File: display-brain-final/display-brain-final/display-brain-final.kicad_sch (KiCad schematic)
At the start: 16 parts, among them J2 Conn_01x05_Socket, J3 Conn_01x19_Socket, J4 Conn_01x19_Socket, J5 Conn_01x04_Socket, J6 Conn_01x07_Socket, J7 Conn_01x02_Socket, P1 USB_C_Plug_USB2.0, U2 ESP32-WROOM-32, U3 AMS1117CD-3.3

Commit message: display brain platine fertig
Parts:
- added C1, C4: 10u, Capacitor_SMD:C_1206_3216Metric_Pad1.33x1.80mm_HandSolder, symbol Device:C_Polarized
- added C2, C3: 1u, Capacitor_SMD:C_1206_3216Metric_Pad1.33x1.80mm_HandSolder, symbol Device:C
- added D1: LED, Diode_SMD:D_1206_3216Metric_Pad1.42x1.75mm_HandSolder, symbol Device:LED
- added R2: 330, Resistor_SMD:R_1206_3216Metric_Pad1.30x1.75mm_HandSolder, symbol Device:R
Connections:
- net 3V3: now also C3.1, C4.1, D1.2 (A)
- net GND: now also C1.2, C2.2, C3.2, C4.2, R2.1
- net at P1.A4 (VBUS), P1.A9 (VBUS), P1.B4 (VBUS)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: now also C1.1, C2.1
- new net: D1.1 (K), R2.2
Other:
- moved on the sheet: J6, J7, U3

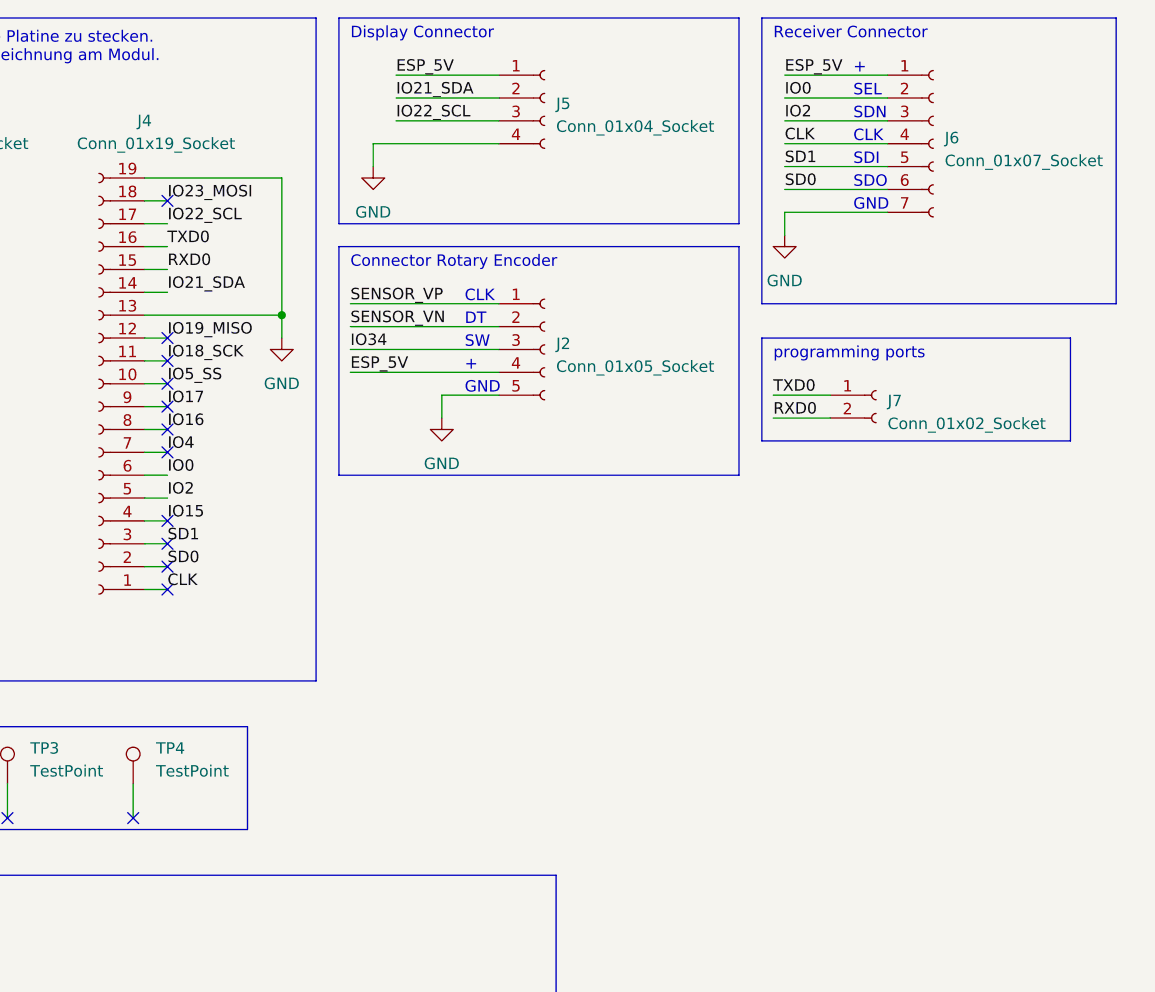
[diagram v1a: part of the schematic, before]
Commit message: display brain platine erweitert
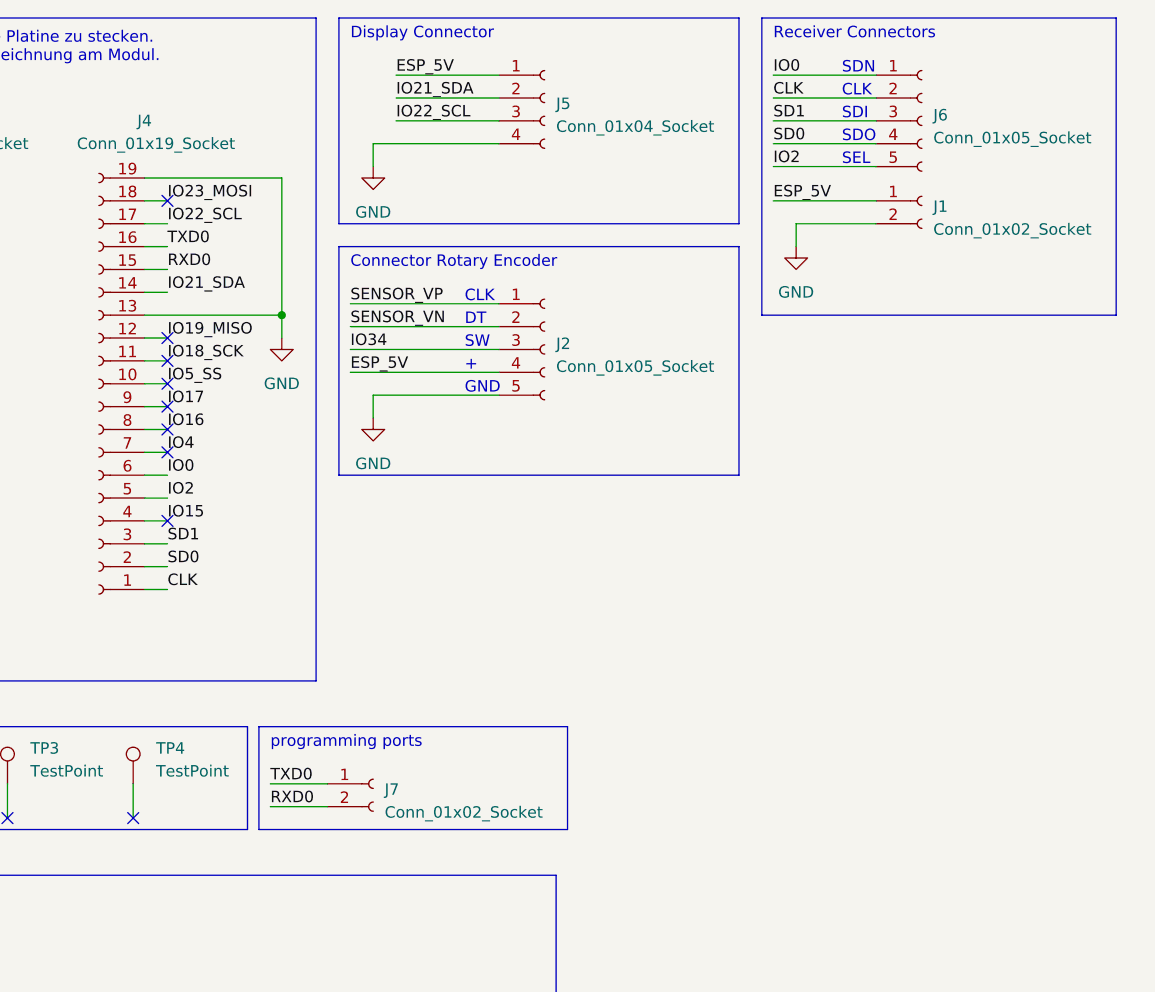
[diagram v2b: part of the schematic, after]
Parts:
- removed J6: Conn_01x07_Socket, Connector_PinSocket_2.54mm:PinSocket_1x07_P2.54mm_Vertical, symbol Connector:Conn_01x07_Socket
- added J1: Conn_01x02_Socket, Connector_PinSocket_2.54mm:PinSocket_1x02_P2.54mm_Vertical, symbol Connector:Conn_01x02_Socket
- added J6: Conn_01x05_Socket, Connector_PinSocket_2.54mm:PinSocket_1x05_P2.54mm_Vertical, symbol Connector:Conn_01x05_Socket
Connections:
- net CLK: now also J6.2 (Pin_2)
- net ESP_5V: now also J1.1 (Pin_1)
- net GND: now also J1.2 (Pin_2)
- net IO0: now also J6.1 (Pin_1)
- net IO2: now also J6.5 (Pin_5)
- net SD0: now also J6.4 (Pin_4)
- net SD1: now also J6.3 (Pin_3)
- no-connect marks 31 -> 28
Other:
- note added: "Receiver Connectors"
- note removed: "Receiver Connector"
- moved on the sheet: J7

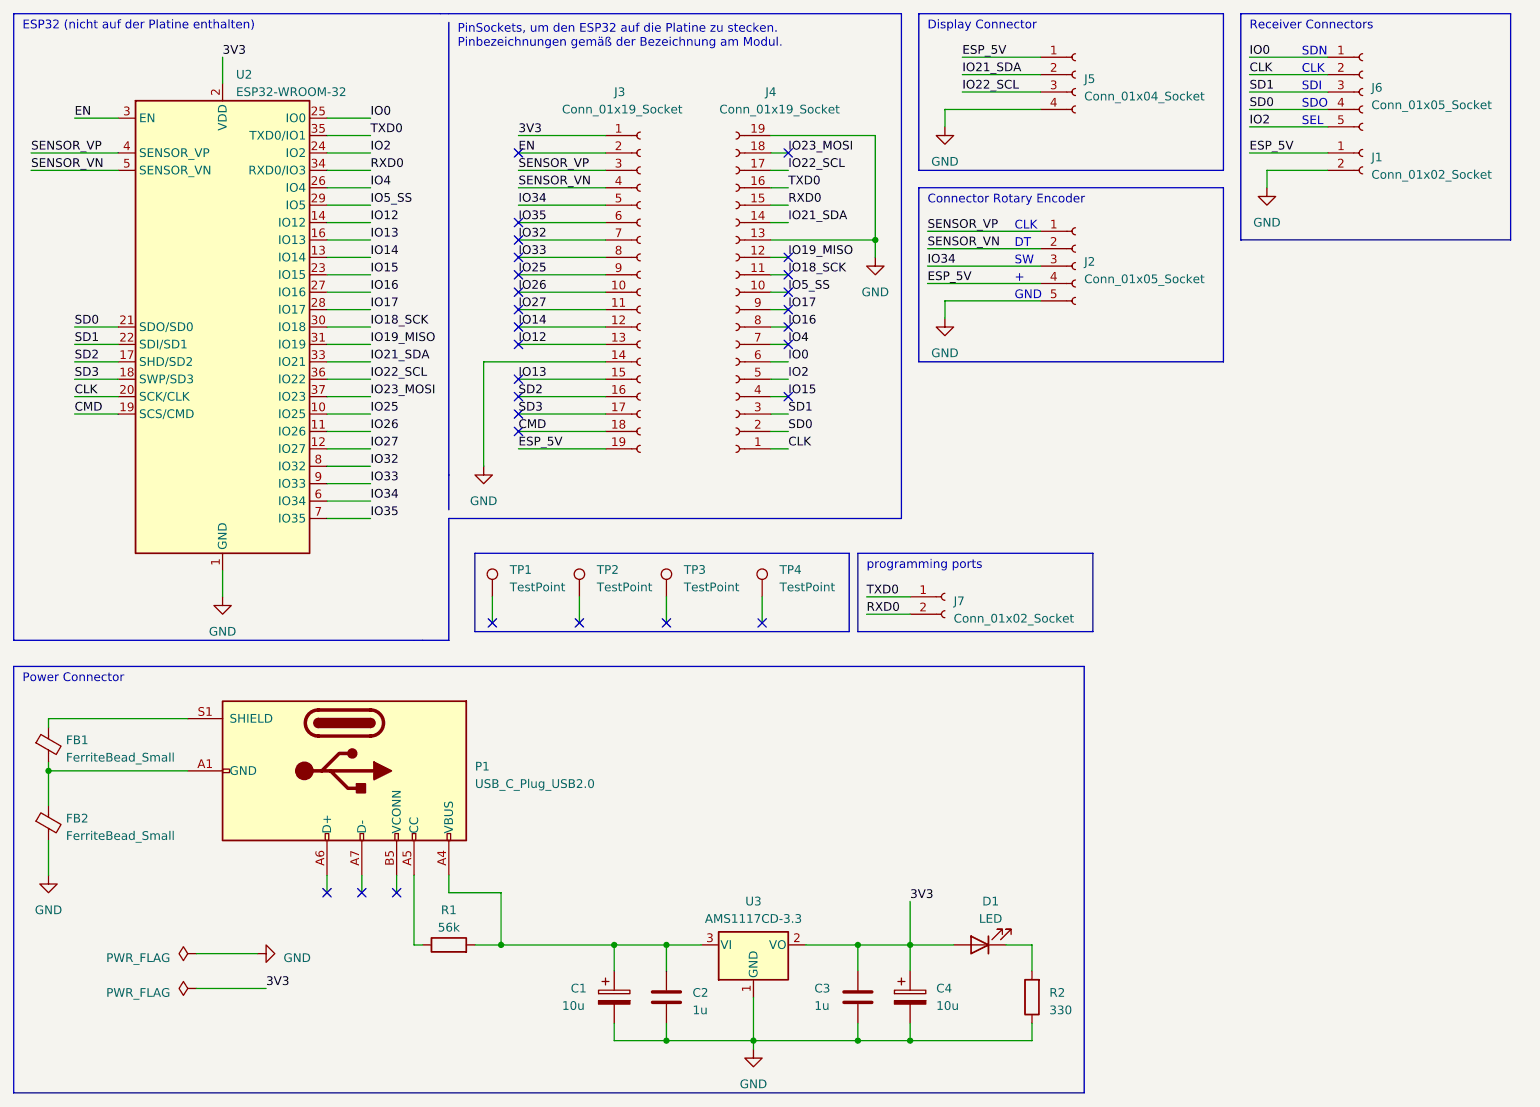
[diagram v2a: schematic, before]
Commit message: 5v versorgung für display geändert
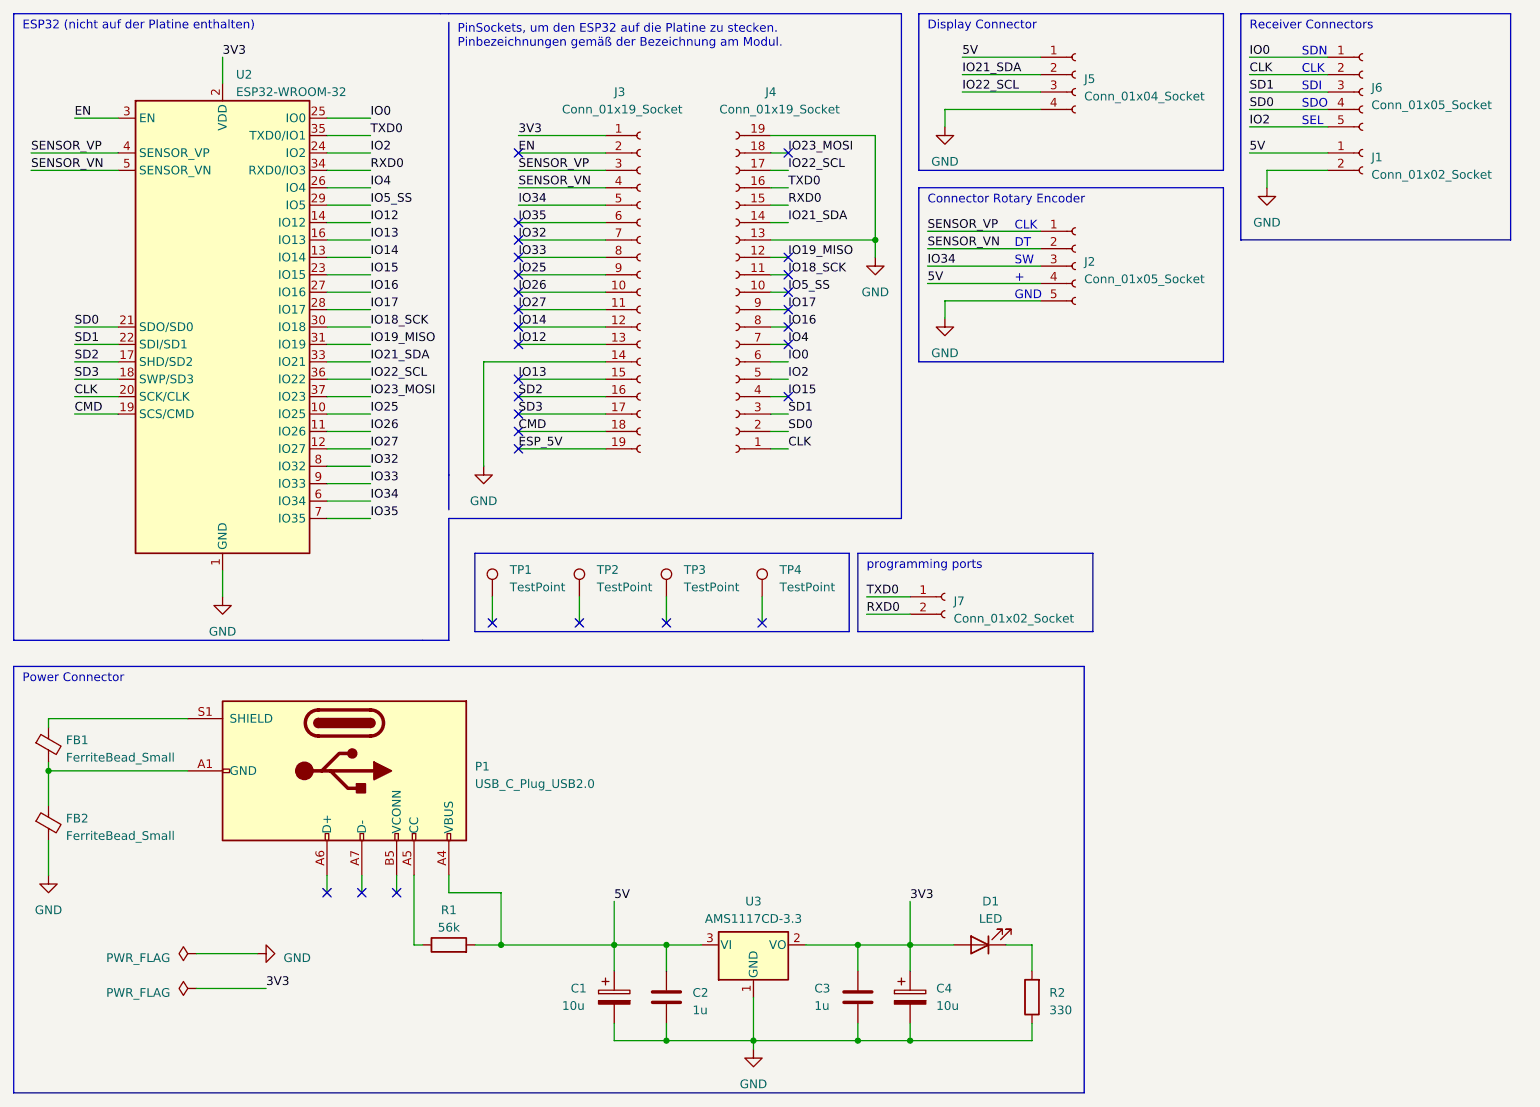
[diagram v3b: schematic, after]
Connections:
- net ESP_5V: no longer J1.1 (Pin_1), J2.4 (Pin_4), J5.1 (Pin_1)
- net 5V: now reaches C1.1, C2.1, P1.A4 (VBUS), P1.A9 (VBUS), P1.B4 (VBUS), P1.B9 (VBUS), R1.2, U3.3 (VI)
- net 5V: now also J1.1 (Pin_1), J2.4 (Pin_4), J5.1 (Pin_1)
- no-connect marks 28 -> 29
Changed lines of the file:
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@@
   (no_connect (at 87.63 34.29))
   (no_connect (at 59.69 142.24))
+  (no_connect (at 87.63 77.47))
   (no_connect (at 87.63 67.31))
   (no_connect (at 87.63 46.99))
@@
     (stroke (width 0) (type default))
   )
+  (wire (pts (xy 101.6 143.51) (xy 101.6 149.86))
+    (stroke (width 0) (type default))
+  )
   (wire (pts (xy 87.63 54.61) (xy 100.33 54.61))
     (stroke (width 0) (type default))
@@
     (effects (font (size 1.27 1.27)) (justify left bottom))
   )
+  (label "5V" (at 101.6 143.51 0) (fields_autoplaced)
+    (effects (font (size 1.27 1.27)) (justify left bottom))
+  )
   (label "IO15" (at 66.04 52.07 0) (fields_autoplaced)
     (effects (font (size 1.27 1.27)) (justify left bottom))
@@
     (effects (font (size 1.27 1.27)) (justify left bottom))
   )
-  (label "ESP_5V" (at 147.32 53.34 0) (fields_autoplaced)
+  (label "5V" (at 147.32 53.34 0) (fields_autoplaced)
     (effects (font (size 1.27 1.27)) (justify left bottom))
   )
@@
     (effects (font (size 1.27 1.27)) (justify left bottom))
   )
-  (label "ESP_5V" (at 152.4 20.32 0) (fields_autoplaced)
+  (label "5V" (at 152.4 20.32 0) (fields_autoplaced)
     (effects (font (size 1.27 1.27)) (justify left bottom))
   )
@@
     (effects (font (size 1.27 1.27)) (justify left bottom))
   )
-  (label "ESP_5V" (at 194.31 34.29 0) (fields_autoplaced)
-    (effects (font (size 1.27 1.27)) (justify left bottom))
-  )
+  (label "5V" (at 194.31 34.29 0) (fields_autoplaced)
+    (effects (font (size 1.27 1.27)) (justify left bottom))
+  )

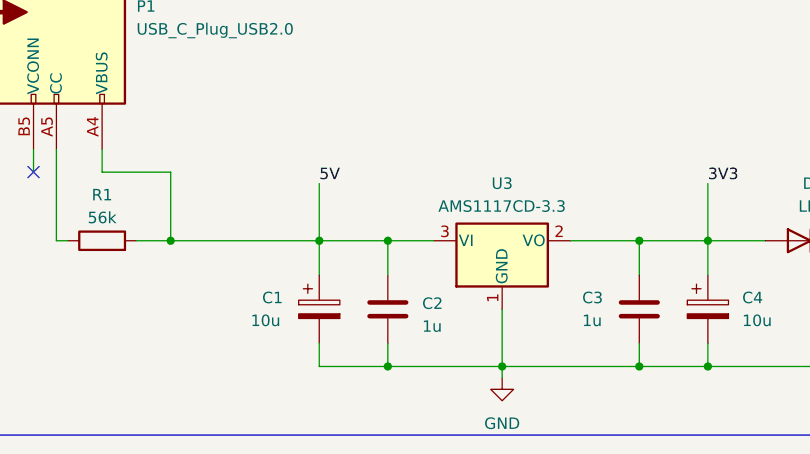
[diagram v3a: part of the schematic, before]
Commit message: Replaced ASM1117 with LM317 in schematic.
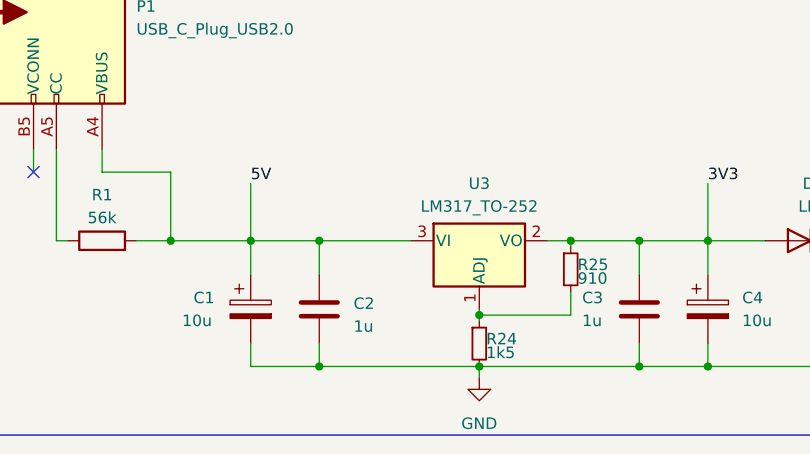
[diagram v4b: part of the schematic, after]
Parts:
- removed U3: AMS1117CD-3.3, Package_TO_SOT_SMD:TO-252-3_TabPin2, symbol Regulator_Linear:AMS1117CD-3.3
- added R24: 1k5, Resistor_SMD:R_1206_3216Metric_Pad1.30x1.75mm_HandSolder, symbol Power-Analyzer-rescue:R_Small
- added R25: 910, Resistor_SMD:R_1206_3216Metric_Pad1.30x1.75mm_HandSolder, symbol Power-Analyzer-rescue:R_Small
- added U3: LM317_TO-252, Package_TO_SOT_SMD:TO-252-2, symbol Regulator_Linear:LM317_TO-252
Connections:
- net 3V3: now also R25.1, U3.2 (VO)
- net 5V: now also U3.3 (VI)
- net GND: now also R24.2
- new net: R24.1, R25.2, U3.1 (ADJ)
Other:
- moved on the sheet: C1, C2

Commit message: Updated PCB layout according to new schematic.(ASM1117-> LM317) (Beidl update)
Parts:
- C2, C3: value 1u -> 100n
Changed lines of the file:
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@@
       (effects (font (size 1.27 1.27)) (justify left))
     )
-    (property "Value" "1u" (at 105.41 159.385 0)
+    (property "Value" "100n" (at 105.41 159.385 0)
       (effects (font (size 1.27 1.27)) (justify left))
     )
@@
       (effects (font (size 1.27 1.27)) (justify left))
     )
-    (property "Value" "1u" (at 130.81 158.75 0)
-      (effects (font (size 1.27 1.27)) (justify left))
-    )
+    (property "Value" "100n" (at 130.81 158.75 0)
+      (effects (font (size 1.27 1.27)) (justify left))
+    )
